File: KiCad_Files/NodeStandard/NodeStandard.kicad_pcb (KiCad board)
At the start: 2 copper layers, 109 parts, among them J1 AC Current In, J10 Opto Coupler 1 in, J11 Opto Coupler 2 in, J12 Opto Coupler 3 in, J13 Relay 1 Output, J14 Relay 2 Output, J15 Schakelaar 3 in, J16 Schakelaar 2 in, J17 Schakelaar 1 in, J18 Force output FET 1 on, J19 Force output FET 2 on, J2 AudioJack3_SwitchTR, J20 FET 1 Output, J21 FET 1 Output, J22 Force output Relay 3 on, J23 Relay 3 Output 1, J24 Relay 3 Output 2, J25 230VAC in, J26 5V-in, J27 ExtDC-in, J3 AC Current loop, J4 EXT1, J5 OledDisplay, J6 RFIDReader, J7 EXT2, J8 Force output Relay 1 on, J9 Force output Relay 2 on, K1 SANYOU_SRD_Form_C, K2 SANYOU_SRD_Form_C, K3 RT42xAxx, Q1 BC547, Q2 BC547, Q3 IRLZ34N, Q4 IRLZ34N, Q5 BC547, U1 MCP23017_SP

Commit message: V0.4 Work in progress, added some footprints with 3D models
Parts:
- removed REF**: 4, MountingHole:MountingHole_3.2mm_M3_DIN965_Pad
- removed REF**: 3, MountingHole:MountingHole_3.2mm_M3_DIN965_Pad
- removed REF**: 2, MountingHole:MountingHole_3.2mm_M3_DIN965_Pad
- removed REF**: 1, MountingHole:MountingHole_3.2mm_M3_DIN965_Pad
- J3: footprint TerminalBlock_RND:TerminalBlock_RND_205-00287_1x02_P5.08mm_Horizontal -> TerminalBlock_Phoenix:TerminalBlock_Phoenix_MKDS-1,5-2-5.08_1x02_P5.08mm_Horizontal
- OK1, OK2, OK3: footprint Footprints:DIL04 -> Package_DIP:DIP-4_W7.62mm
- moved OK1 4.02 mm to (134.6, 138.4), turned to 180 degrees
- moved OK2 4.02 mm to (134.6, 116.8), turned to 180 degrees
- moved OK3 4.02 mm to (134.6, 95.2), turned to 180 degrees

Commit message: V0.5 Work in progress, first version  PCB design, no silk screen yet
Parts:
- added J28: Hal current sensor, TerminalBlock_Phoenix:TerminalBlock_Phoenix_MPT-0,5-3-2.54_1x03_P2.54mm_Horizontal, F.Cu at (36.8, 86.4)
- added J29: Current sensor select, Connector_PinHeader_2.54mm:PinHeader_1x03_P2.54mm_Vertical, F.Cu at (73.7, 119.4)
- added REF**: MountingHole_3.2mm_M3, MountingHole:MountingHole_3.2mm_M3, F.Cu at (97.2, 167.6)
- added REF**: MountingHole_3.2mm_M3, MountingHole:MountingHole_3.2mm_M3, F.Cu at (152.4, 26.7)
- added REF**: MountingHole_3.2mm_M3, MountingHole:MountingHole_3.2mm_M3, F.Cu at (34.9, 26.7)
- J15, J16, J17: footprint Connector_Phoenix_MSTB:PhoenixContact_MSTB_2,5_2-GF-5,08_1x02_P5.08mm_Horizontal_ThreadedFlange -> TerminalBlock_Phoenix:TerminalBlock_Phoenix_MPT-0,5-2-2.54_1x02_P2.54mm_Horizontal
- J5, J6: footprint Connector_Phoenix_MSTB:PhoenixContact_MSTB_2,5_4-GF-5,08_1x04_P5.08mm_Horizontal_ThreadedFlange -> TerminalBlock_Phoenix:TerminalBlock_Phoenix_MPT-0,5-4-2.54_1x04_P2.54mm_Horizontal
- JP1, JP2, JP3, JP4, JP5, JP8: footprint Jumper:SolderJumper-2_P1.3mm_Open_RoundedPad1.0x1.5mm -> Footprints:SolderJumper-2_P3mm_Open_RoundedPad
- moved C1 70.0 mm to (114.3, 94.0), turned to 0 degrees
- moved C8 36.4 mm to (144.8, 64.8), turned to 270 degrees
- moved J6 34.7 mm to (118.1, 170.2)
- moved R3 25.3 mm to (92.7, 153.7)
- moved R1 25.2 mm to (134.6, 155.6), turned to 270 degrees
- moved Q1 24.3 mm to (111.8, 72.4)
- moved J17 23.7 mm to (36.8, 71.1)
- moved R5 21.7 mm to (92.7, 143.5)
- moved R4 20.5 mm to (100.3, 139.7)
- moved J25 20.5 mm to (144.8, 52.1), turned to 90 degrees
- moved C9 20.5 mm to (73.7, 73.7)
- moved D5 20.5 mm to (100.3, 62.2)
- moved D6 20.5 mm to (73.7, 62.2)
- moved R10 20.5 mm to (83.8, 73.7)
- moved R11 20.5 mm to (100.3, 67.3)
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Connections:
- D1 pad 2: GPI35 -> Net-(D1-Pad2)
- D2 pad 1: GPI35 -> Net-(D1-Pad2)
- J25 pad 1: 230VAC-L -> 230VAC-N
- J25 pad 2: 230VAC-N -> 230VAC-L
- R3 pad 1: GPI35 -> Net-(D1-Pad2)
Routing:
- net GND: track 0.00 -> 661.1 mm
- net +5V: track 0.00 -> 292.8 mm
- net +3V3: track 0.00 -> 279.6 mm
- net GPIO32: track 0.00 -> 225.6 mm
- net FET2: track 0.00 -> 219.7 mm
- net GPIO13_I2C-SDA: track 0.00 -> 202.1 mm
- net GPIO16_I2C-SCL: track 0.00 -> 151.4 mm
- net Net-(J28-Pad3): track 0.00 -> 147.8 mm
- net 230VAC-L: track 0.00 -> 127.6 mm
- net Net-(C1-Pad1): track 0.00 -> 111.6 mm
- net 230VAC-N: track 0.00 -> 102.4 mm
- net ExternalDCPower: track 0.00 -> 101.1 mm
- net GPI36_U1RXD: track 0.00 -> 94.8 mm
- net FET1: track 0.00 -> 92.4 mm
- net GPIO33: track 0.00 -> 81.6 mm
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- added copper zone on B.Cu, net GND
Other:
- board outline added: 129 x 156.7 mm

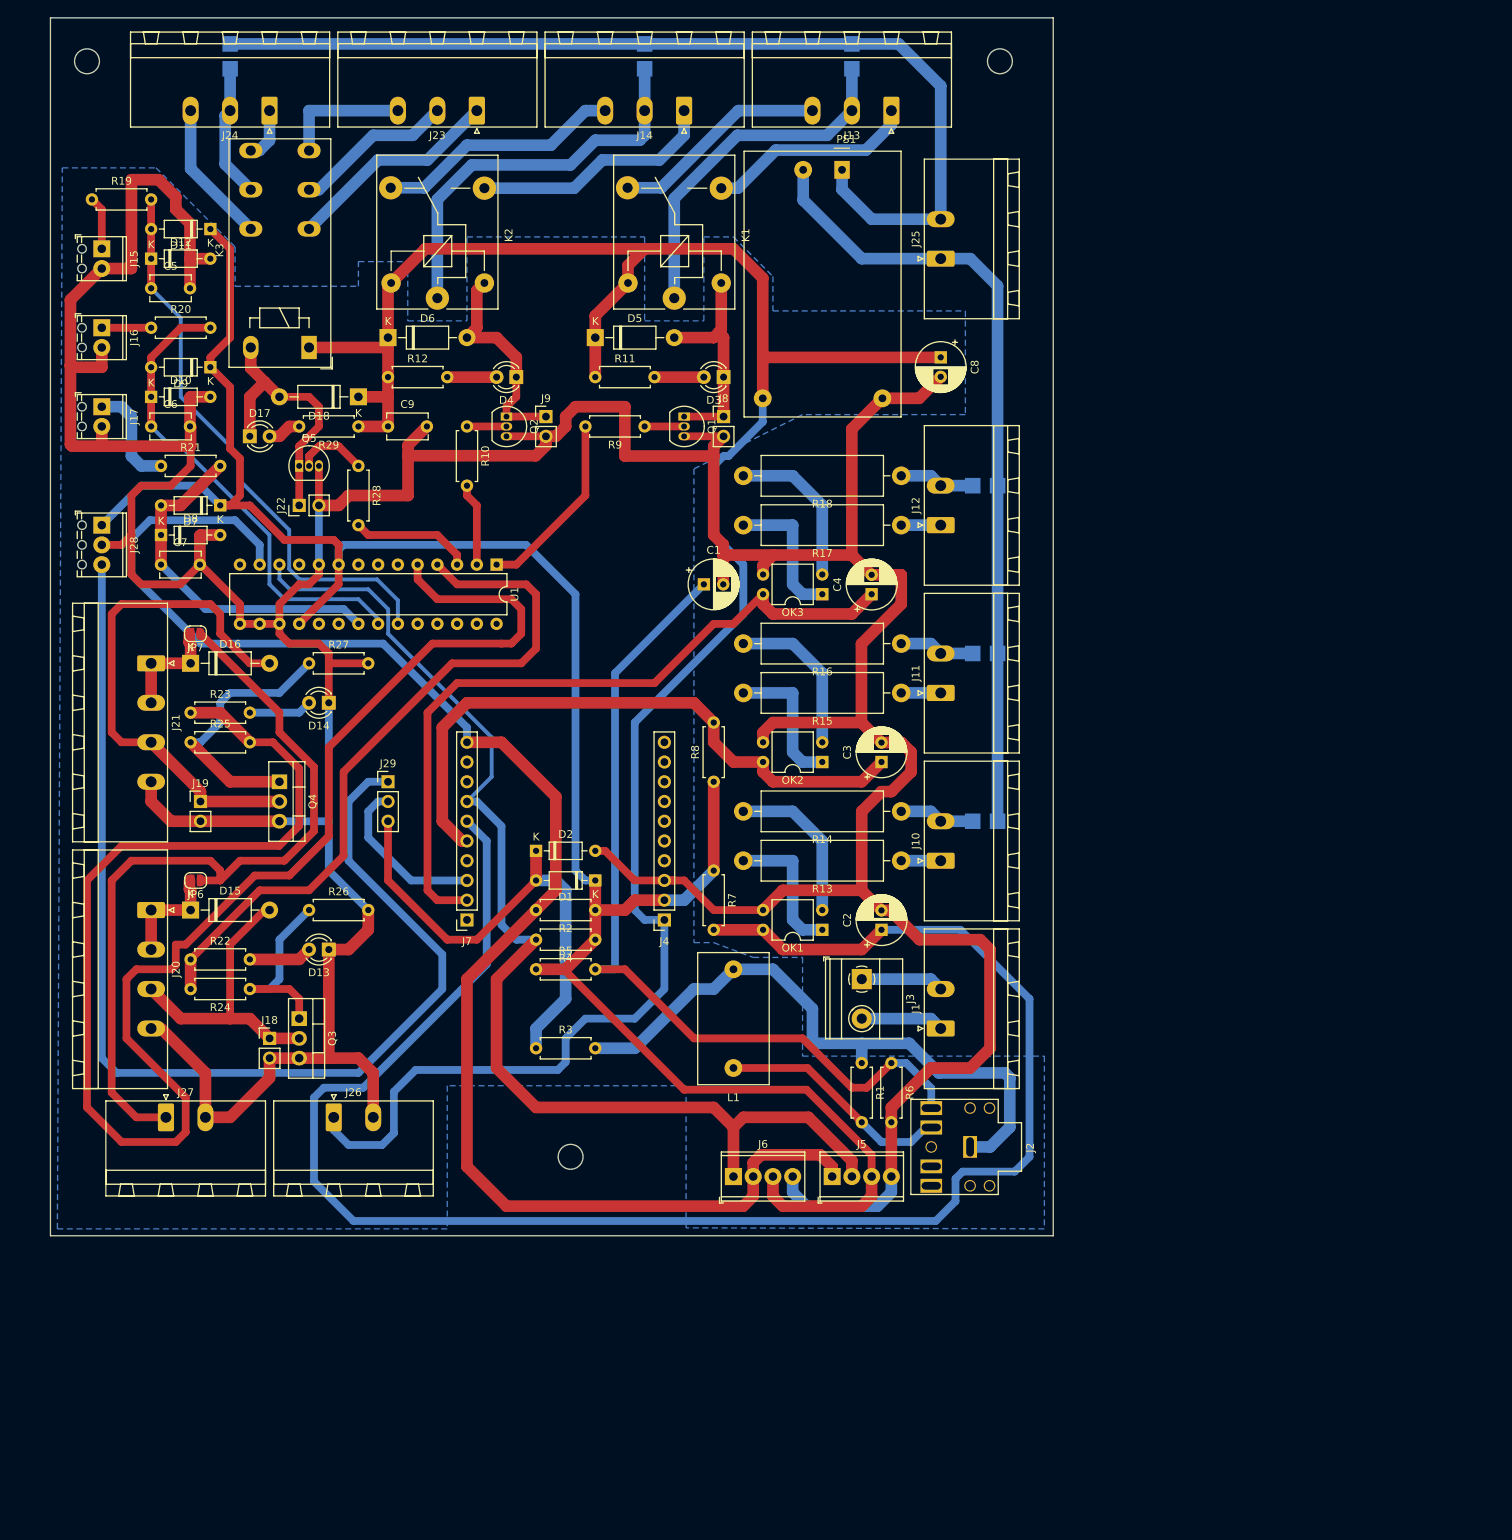
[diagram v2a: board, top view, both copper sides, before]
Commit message: V0.6 Silk screen added, ready for first trial with real print
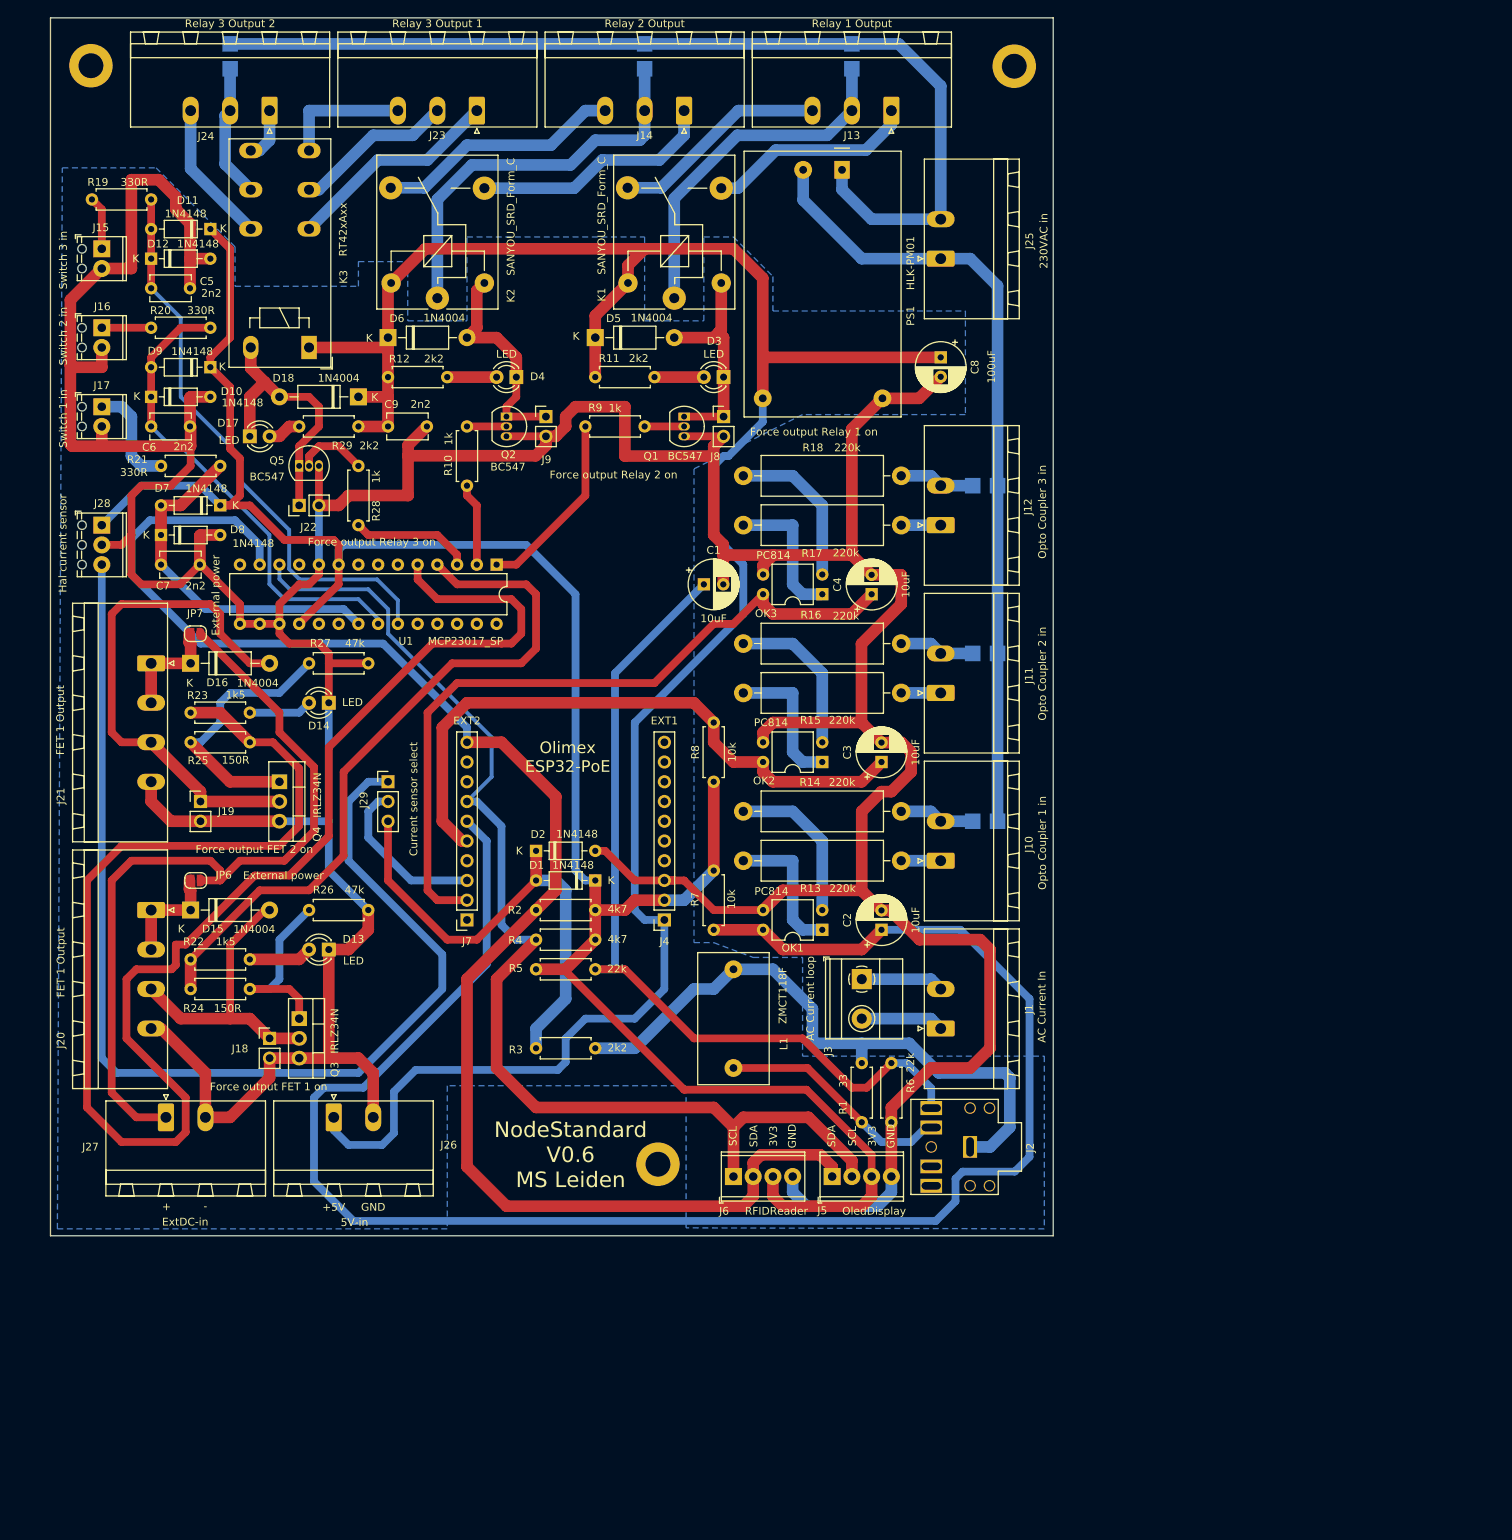
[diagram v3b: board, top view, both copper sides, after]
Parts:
- removed the REF** at (97.2, 167.6)
- removed the REF** at (152.4, 26.7)
- removed the REF** at (34.9, 26.7)
- added REF**: MountingHole_3.2mm_M3_DIN965_Pad, MountingHole:MountingHole_3.2mm_M3_DIN965_Pad, F.Cu at (108.4, 168.6)
- added REF**: MountingHole_3.2mm_M3_DIN965_Pad, MountingHole:MountingHole_3.2mm_M3_DIN965_Pad, F.Cu at (154.2, 27.3)
- added REF**: MountingHole_3.2mm_M3_DIN965_Pad, MountingHole:MountingHole_3.2mm_M3_DIN965_Pad, F.Cu at (35.4, 27.2)
- J15: value Schakelaar 3 in -> Switch 3 in
- J16: value Schakelaar 2 in -> Switch 2 in
- J17: value Schakelaar 1 in -> Switch 1 in
- J2: value AudioJack3_SwitchTR -> Current coil in
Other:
- board text added: "+"
- board text added: "+5V"
- board text added: "-"
- board text added: "3V3"
- board text added: "GND"
- board text added: "NodeStandard V0.6 MS Leiden"
- board text added: "Olimex ESP32-PoE"
- board text added: "SCL"
- board text added: "SDA"

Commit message: V0.7 a few changes needed for the production of the PCB
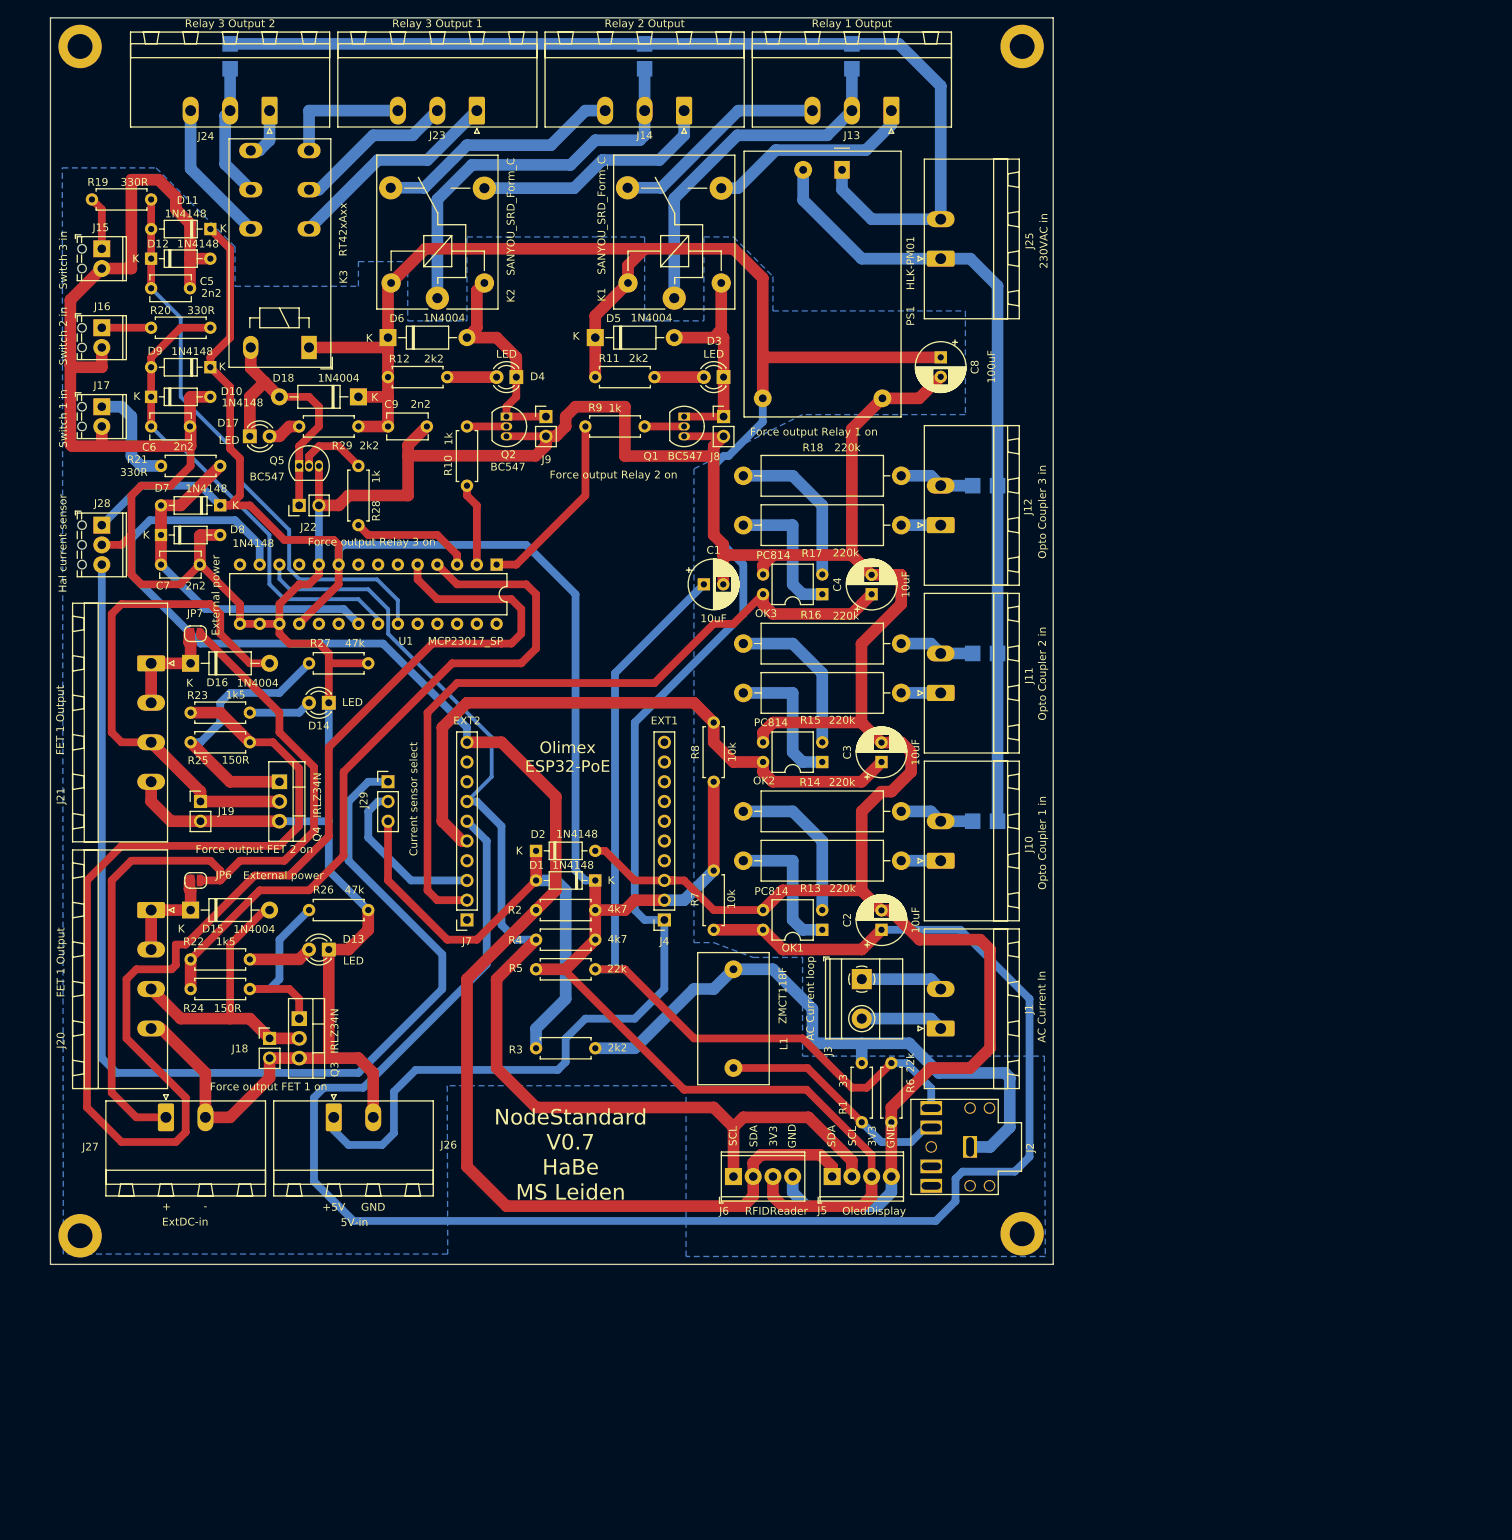
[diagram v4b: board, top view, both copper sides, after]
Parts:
- added REF**: MountingHole_3.2mm_M3_DIN965_Pad, MountingHole:MountingHole_3.2mm_M3_DIN965_Pad, F.Cu at (155.3, 177.5)
- moved REF** 74.9 mm to (34.0, 177.8)
- moved REF** 2.84 mm to (34.0, 24.8)
- moved REF** 2.74 mm to (155.3, 24.8)
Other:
- board size 129 x 156.7 mm -> 129 x 160.4 mm
- board text added: "NodeStandard V0.7 HaBe MS Leiden"
- board text removed: "NodeStandard V0.6 MS Leiden"

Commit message: V0.8 moved a mounting hole and generated Gerber files
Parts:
- moved REF** 0.25 mm to (34.0, 177.5)
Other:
- board text added: "NodeStandard V0.8 HaBe MS Leiden"
- board text removed: "NodeStandard V0.7 HaBe MS Leiden"

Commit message: Version 0.9: 2 typo's in silkscreen labels corrected
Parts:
- J21: value FET 1 Output -> FET 2 Output
- L1: value ZMCT118F -> TA12
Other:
- board text added: "NodeStandard V0.9 HaBe MS Leiden"
- board text removed: "NodeStandard V0.8 HaBe MS Leiden"
